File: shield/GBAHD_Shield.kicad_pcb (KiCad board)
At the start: 2 copper layers, 49 x 39 mm, 18 parts, among them J1 Conn_01x40, J2 Conn_02x08_Top_Bottom, J3 Conn_01x16, J4 Conn_02x10_Top_Bottom, J5 Conn_01x05, J6 Conn_02x03_Odd_Even, J7 Conn_01x01, SW1 SW_Push, U1 SNES_7PIN, U2 ATmega328P-AU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

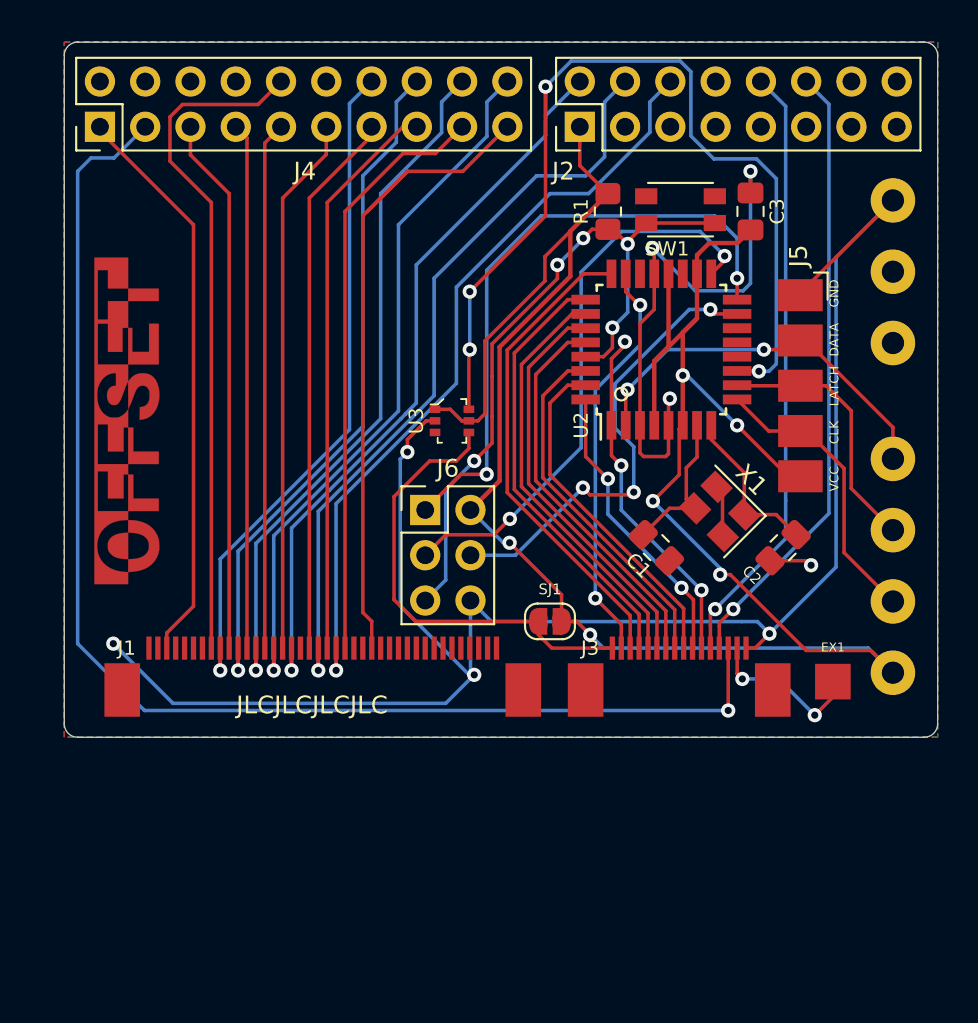
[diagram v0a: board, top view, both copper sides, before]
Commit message: Version 2 initial commit.
- Changed board layout
- Changed breakout board pin order
- Changed FFC connectors
- Added connectors for 32 pin and 34 pin
- Changed SNES connector to Classic connector.
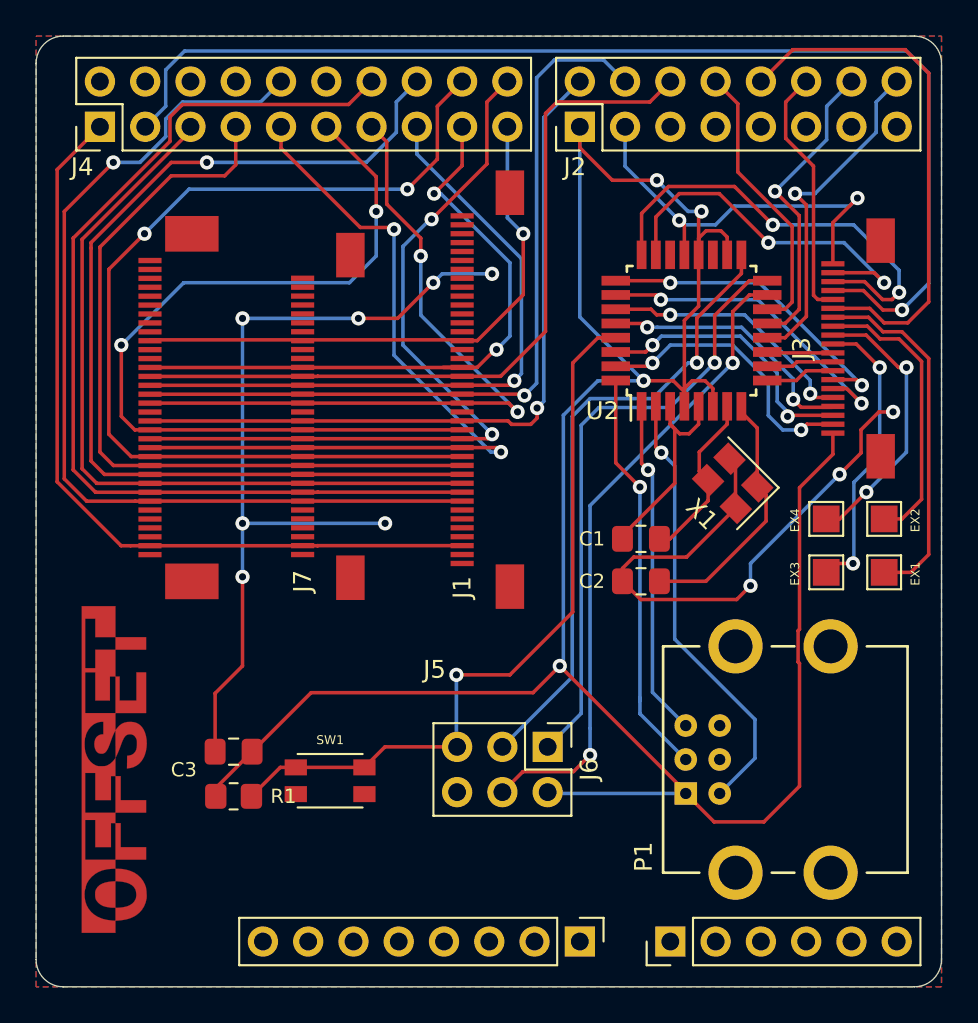
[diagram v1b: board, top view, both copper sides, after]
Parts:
- removed the G*** at (47.7, 47.8)
- removed SJ1: SOLDER_JUMPER, Jumper:SolderJumper-2_P1.3mm_Open_RoundedPad1.0x1.5mm
- removed U1: SNES_7PIN, OFFSET:SNES_7PIN
- removed U3: WAS3157B, OFFSET:SOT-363
- added G***: LOGO, Raizu_OFFSET:OFFSET_LOGO_4.0mm, F.Cu at (47.0, 67.3)
- added P1: CONN_WII, Raizu_OFFSET:CONN_WII, F.Cu at (84.5, 66.8)
- added REF**: PinHeader_1x06_P2.54mm_Vertical, Connector_PinHeader_2.54mm:PinHeader_1x06_P2.54mm_Vertical, F.Cu at (78.0, 77.0)
- added REF**: PinHeader_1x08_P2.54mm_Vertical, Connector_PinHeader_2.54mm:PinHeader_1x08_P2.54mm_Vertical, F.Cu at (72.9, 77.0)
- added TP1: EX1, TestPoint:TestPoint_Pad_1.5x1.5mm, F.Cu at (90.0, 56.2)
- added TP2: EX2, TestPoint:TestPoint_Pad_1.5x1.5mm, F.Cu at (90.0, 53.2)
- added TP3: EX3, TestPoint:TestPoint_Pad_1.5x1.5mm, F.Cu at (86.8, 56.2)
- added TP4: EX4, TestPoint:TestPoint_Pad_1.5x1.5mm, F.Cu at (86.8, 53.2)
- J1: footprint OFFSET:JUSHUO_AFC07-S40FCC-00 -> Raizu:JUSHUO_AFC01-S40FCC-00
- J3: value Conn_01x16 -> Conn_01x20; footprint OFFSET:JUSHUO_AFC07-S16FCC-00 -> Raizu:JUSHUO_AFC01-S20FCC-00
- J5: value Conn_01x05 -> Conn_01x34; footprint OFFSET:Pads_01x05 -> Raizu:JUSHUO_AFC07-S34FCC-00
- J7: value Conn_01x01 -> Conn_01x32; footprint OFFSET:SOLDER_PAD -> Raizu:JUSHUO_AFC01-S32FCC-00
- SW1: footprint OFFSET:XKB-TS-1185EC-C-D-B -> Raizu_OFFSET:XKB-TS-1185EC-C-D-B
- moved C3 41.9 mm to (53.5, 66.3), turned to 0 degrees
- moved R1 39.0 mm to (53.5, 68.8), turned to 0 degrees
- moved SW1 37.6 mm to (58.9, 67.9), turned to 0 degrees
- moved J5 34.5 mm to (50.6, 47.0), turned to 90 degrees
- moved J7 33.2 mm to (57.4, 47.5), turned to 90 degrees
- moved J3 20.5 mm to (87.1, 43.7), turned to 90 degrees
- moved J1 17.9 mm to (66.3, 46.5), turned to 90 degrees
- moved J6 15.0 mm to (71.1, 66.0), turned to 270 degrees
- moved C2 8.19 mm to (76.4, 56.8), turned to 0 degrees
- moved U2 2.00 mm to (79.2, 42.7)
- moved X1 1.74 mm to (81.5, 51.2)
- moved C1 0.99 mm to (76.4, 54.4), turned to 0 degrees
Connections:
- C3 pad 2: SP_3V3 -> GBA_VCC
- J2 pad 1: SP_3V3 -> GBA_VCC
- J3 pad 10: GBA_START -> GBA_RESET
- J3 pad 11: GBA_SELECT -> Net-(J3-Pad11)
- J3 pad 12: GBA_AUD2 -> Net-(J3-Pad12)
- J3 pad 13: GBA_AUD1 -> Net-(J3-Pad13)
- J3 pad 14: GBA_CLK -> Net-(J3-Pad14)
- J3 pad 15: Net-(J3-Pad15) -> GBA_AUD2
- J3 pad 16: GND -> GBA_AUD1
- J3 pad 2: GBA_UP -> GBA_R
- J3 pad 3: GBA_DOWN -> GBA_L
- J3 pad 4: GBA_LEFT -> GBA_B
- J3 pad 5: GBA_RGHT -> GBA_A
- J3 pad 6: GBA_A -> GBA_RGHT
- J3 pad 7: GBA_B -> GBA_LEFT
- J3 pad 8: GBA_L -> GBA_START
- J3 pad 9: GBA_R -> GBA_SELECT
- J5 pad 1: GND -> Net-(J5-Pad1)
- J5 pad 2: SNS_DATA -> GB_DCLK
- J5 pad 3: SNS_LATCH -> Net-(J5-Pad3)
- J5 pad 4: SNS_CLK -> Net-(J5-Pad4)
- J5 pad 5: SP_3V3 -> Net-(J5-Pad5)
- J6 pad 2: SP_3V3 -> GBA_VCC
- J7 pad 1: Net-(J3-Pad15) -> Net-(J7-Pad1)
- R1 pad 1: SP_3V3 -> GBA_VCC
- U2 pad 1: GBA_SELECT -> JOY_SDA
- U2 pad 10: SNS_LATCH -> GBA_SELECT
- U2 pad 11: GBA_POWER_SEL -> GBA_RESET
- U2 pad 12: Net-(U2-Pad12) -> SP_ARD0
- U2 pad 13: Net-(U2-Pad13) -> SP_ARD1
- U2 pad 14: Net-(U2-Pad14) -> SP_ARD4
- U2 pad 18: SP_3V3 -> GBA_VCC
- U2 pad 2: SNS_DATA -> JOY_SCL
- U2 pad 20: SP_3V3 -> GBA_VCC
- U2 pad 32: GBA_START -> JOY_DET
- U2 pad 4: SP_3V3 -> GBA_VCC
- U2 pad 6: SP_3V3 -> GBA_VCC
- U2 pad 9: SNS_CLK -> GBA_START
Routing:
- net SP_3V3: track 126.4 -> 0.00 mm, vias 6 -> 0
- net GBA_VCC: track 25.8 -> 136.2 mm, vias 0 -> 4
- net GBA_POWER_SEL: track 52.9 -> 0.00 mm, vias 4 -> 0
- net JOY_SCL: track 0.00 -> 25.1 mm, vias 0 -> 1
- net JOY_DET: track 0.00 -> 23.1 mm, vias 0 -> 1
- net SNS_DATA: track 21.9 -> 0.00 mm, vias 2 -> 0
- net GBA_AUD1: track 34.9 -> 14.3 mm, vias 1 -> 0
- net Net-(J3-Pad14): track 0.00 -> 20.2 mm
- net SP_ARD0: track 0.00 -> 19.2 mm, vias 0 -> 1
- net JOY_SDA: track 0.00 -> 18.9 mm, vias 0 -> 1
- net GB_R4: track 37.8 -> 56.5 mm, vias 1 -> 0
- net GB_R2: track 38.4 -> 56.4 mm
- net GND: track 134.3 -> 116.4 mm, vias 8 -> 12
- net GB_G2: track 30.3 -> 48.2 mm, vias 0 -> 2
- net SP_ARD1: track 0.00 -> 17.2 mm, vias 0 -> 1
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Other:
- board size 49 x 39 mm -> 50.8 x 53.3 mm
- board text removed: "CLK"
- board text removed: "DATA"
- board text removed: "Designed in México"
- board text removed: "EX1"
- board text removed: "GND"
- board text removed: "JLCJLCJLCJLC"
- board text removed: "LATCH"
- board text removed: "Raizu 2020"
- board text removed: "VCC"
- board text removed: "gbaHD Shield"

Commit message: PCB changes and breakout board
- Added breakout to main board as a breakaway board.
- Added controller connector expansion for port relocation
- Tidying routing and other minimal changes
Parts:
- removed the REF** at (72.9, 77.0)
- added CLK: GBA_CLK, Raizu_OFFSET:SOLDER_PAD, F.Cu at (21.8, 77.9)
- added GEX1: GBA_EX1, Raizu_OFFSET:SOLDER_PAD, F.Cu at (29.4, 61.0)
- added GEX2: GBA_EX2, Raizu_OFFSET:SOLDER_PAD, F.Cu at (22.0, 67.4)
- added GEX3: GBA_EX3, Raizu_OFFSET:SOLDER_PAD, F.Cu at (22.0, 70.0)
- added GEX4: GBA_EX4, Raizu_OFFSET:SOLDER_PAD, F.Cu at (22.0, 68.7)
- added GND: GBA_GND, Raizu_OFFSET:SOLDER_PAD, F.Cu at (24.1, 63.5)
- added J8: Conn_01x05, Connector_PinHeader_2.54mm:PinHeader_1x05_P2.54mm_Vertical, F.Cu at (42.1, 38.9)
- added J9: Conn_01x20, Raizu:JUSHUO_AFC01-S20FCC-00, F.Cu at (31.7, 69.5)
- added JP1: Jumper_NC_Small, Jumper:SolderJumper-2_P1.3mm_Bridged_RoundedPad1.0x1.5mm, B.Cu at (90.2, 34.8)
- added JP2: Jumper_NC_Small, Jumper:SolderJumper-2_P1.3mm_Bridged_RoundedPad1.0x1.5mm, B.Cu at (87.2, 34.8)
- added JP3: Jumper_NC_Small, Jumper:SolderJumper-2_P1.3mm_Bridged_RoundedPad1.0x1.5mm, B.Cu at (81.8, 34.8)
- added RESET: GBA_RESET, Raizu_OFFSET:SOLDER_PAD, F.Cu at (24.3, 75.0)
- added S01: GBA_S01, Raizu_OFFSET:SOLDER_PAD, F.Cu at (27.4, 61.0)
- added S02: GBA_S02, Raizu_OFFSET:SOLDER_PAD, F.Cu at (28.4, 63.5)
- added TP0: GBA_A, Raizu_OFFSET:SOLDER_PAD, F.Cu at (25.4, 61.0)
- added TP1: GBA_B, Raizu_OFFSET:SOLDER_PAD, F.Cu at (26.4, 63.5)
- added TP2: GBA_SEL, Raizu_OFFSET:SOLDER_PAD, F.Cu at (28.6, 77.6)
- added TP3: GBA_STR, Raizu_OFFSET:SOLDER_PAD, F.Cu at (26.9, 77.6)
- added TP4: GBA_DR, Raizu_OFFSET:SOLDER_PAD, F.Cu at (26.0, 75.0)
- added TP5: GBA_DL, Raizu_OFFSET:SOLDER_PAD, F.Cu at (23.5, 77.6)
- added TP6: GBA_DU, Raizu_OFFSET:SOLDER_PAD, F.Cu at (25.2, 77.6)
- added TP7: GBA_DD, Raizu_OFFSET:SOLDER_PAD, F.Cu at (27.7, 75.0)
- added TP8: GBA_R, Raizu_OFFSET:SOLDER_PAD, F.Cu at (23.4, 61.0)
- added TP9: GBA_L, Raizu_OFFSET:SOLDER_PAD, F.Cu at (22.6, 75.0)
- added VCC: GBA_VCC, Raizu_OFFSET:SOLDER_PAD, F.Cu at (30.3, 77.3)
- added mouse-bite-2.54mm-slot: VAL**, Panelization:mouse-bite-2.54mm-slot, F.Cu at (38.5, 64.2)
- added mouse-bite-2.54mm-slot: VAL**, Panelization:mouse-bite-2.54mm-slot, F.Cu at (38.5, 74.8)
- moved G*** 2.75 mm to (44.2, 67.5)
- renumbered TP1 to EX1, TP2 to EX2, TP3 to EX3, TP4 to EX4
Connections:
- U2 pad 12: SP_ARD0 -> Net-(JP1-Pad1)
- U2 pad 13: SP_ARD1 -> Net-(JP2-Pad1)
- U2 pad 14: SP_ARD4 -> Net-(JP3-Pad1)
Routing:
- net JOY_SDA: track 18.9 -> 80.2 mm, vias 1 -> 2
- net JOY_SCL: track 25.1 -> 85.4 mm, vias 1 -> 2
- net JOY_DET: track 23.1 -> 82.4 mm, vias 1 -> 2
- net GBA_VCC: track 136.2 -> 169.7 mm, vias 4 -> 5
- net Net-(J9-Pad2): track 0.00 -> 31.2 mm, vias 0 -> 2
- net Net-(GBA3-Pad1): track 0.00 -> 30.7 mm, vias 0 -> 2
- net Net-(J9-Pad19): track 0.00 -> 28.4 mm, vias 0 -> 2
- net Net-(J9-Pad5): track 0.00 -> 23.5 mm, vias 0 -> 2
- net Net-(GEX1-Pad1): track 0.00 -> 19.3 mm, vias 0 -> 2
- net Net-(J9-Pad16): track 0.00 -> 17.8 mm, vias 0 -> 2
- net Net-(J9-Pad18): track 0.00 -> 16.5 mm, vias 0 -> 2
- net Net-(JP1-Pad1): track 0.00 -> 16.4 mm, vias 0 -> 1
- net Net-(J9-Pad15): track 0.00 -> 15.6 mm, vias 0 -> 2
- net GND: track 116.4 -> 130.2 mm, vias 12 -> 17
- net Net-(J9-Pad3): track 0.00 -> 13.7 mm, vias 0 -> 2
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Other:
- board size 50.8 x 53.3 mm -> 72.3 x 53.3 mm
- board text added: "JLCJLCJLCJLC"
- board text added: "Raizu 2021 Designed in México"
- board text added: "gbaHD Shield"

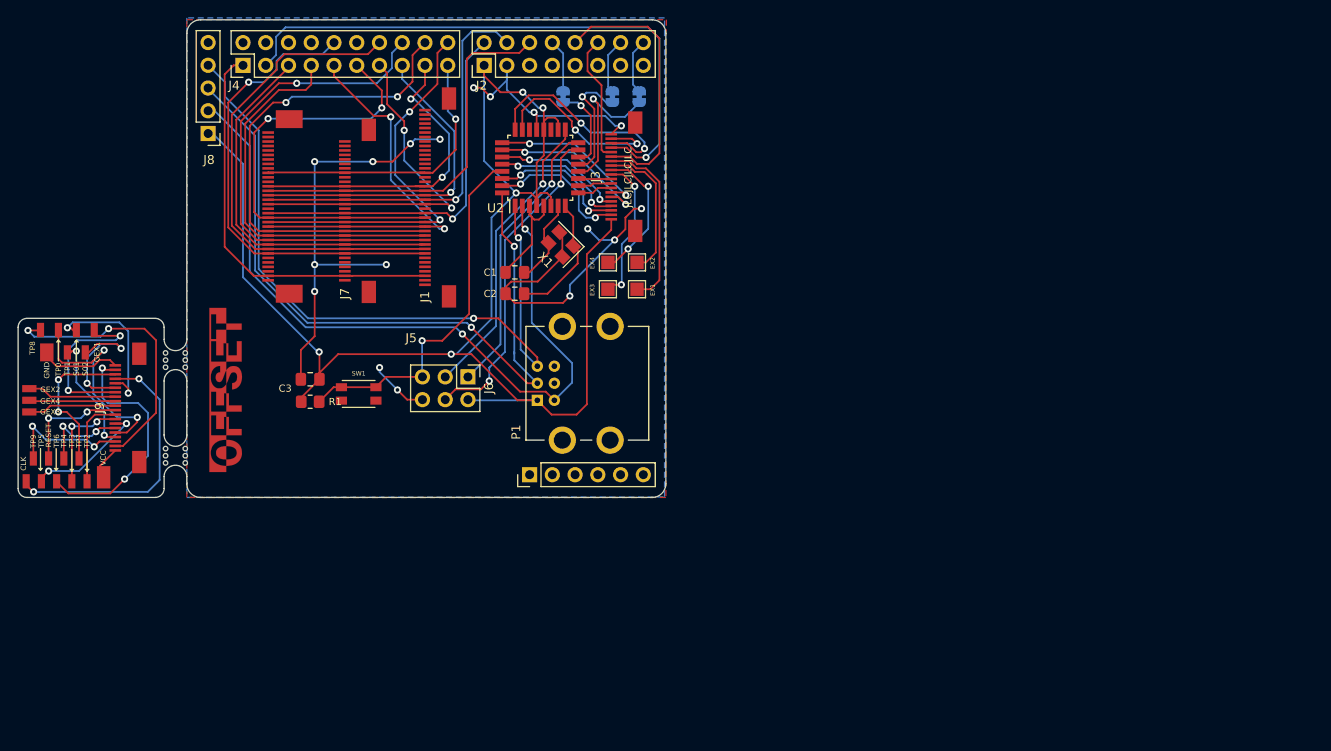
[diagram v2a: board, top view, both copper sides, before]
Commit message: PCB design work
- Added extension board (controller, LED and power switch)
- Panelized board
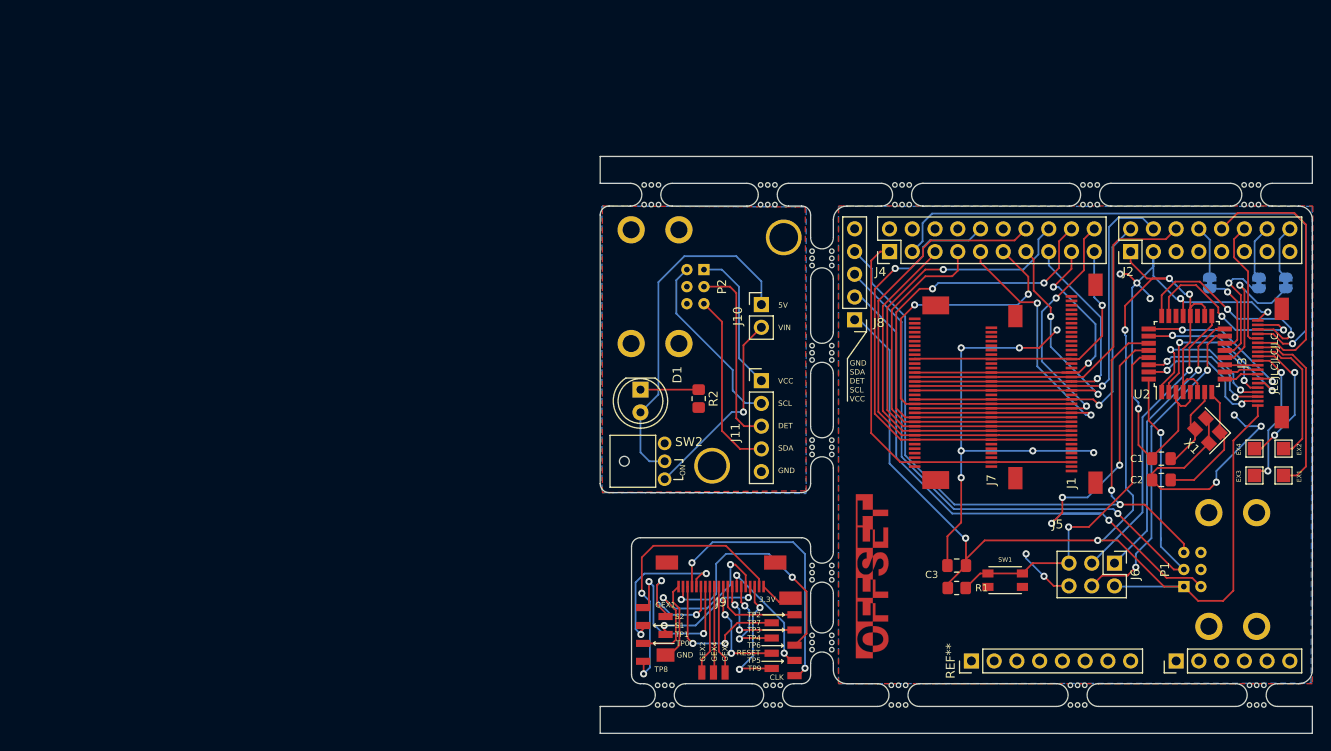
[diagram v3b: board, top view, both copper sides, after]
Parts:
- removed CLK: GBA_CLK, Raizu_OFFSET:SOLDER_PAD
- removed GND: GBA_GND, Raizu_OFFSET:SOLDER_PAD
- removed RESET: GBA_RESET, Raizu_OFFSET:SOLDER_PAD
- removed S01: GBA_S01, Raizu_OFFSET:SOLDER_PAD
- removed S02: GBA_S02, Raizu_OFFSET:SOLDER_PAD
- removed VCC: GBA_VCC, Raizu_OFFSET:SOLDER_PAD
- removed the mouse-bite-2.54mm-slot at (38.5, 64.2)
- removed the mouse-bite-2.54mm-slot at (38.5, 74.8)
- added D1: LED, LED_THT:LED_D5.0mm_FlatTop, F.Cu at (90.4, 67.5)
- added GBA1: GBA_VCC, Raizu_OFFSET:SOLDER_PAD, F.Cu at (107.1, 90.9)
- added GBA2: GBA_RESET, Raizu_OFFSET:SOLDER_PAD, F.Cu at (104.9, 96.9)
- added GBA3: GBA_CLK, Raizu_OFFSET:SOLDER_PAD, F.Cu at (107.7, 99.4)
- added GBA4: GBA_GND, Raizu_OFFSET:SOLDER_PAD, F.Cu at (93.3, 97.1)
- added HOLE_M3: VAL**, keyboard_parts:HOLE_M3, F.Cu at (98.4, 76.0)
- added HOLE_M3: VAL**, keyboard_parts:HOLE_M3, F.Cu at (106.4, 50.5)
- added J10: Conn_01x02, Connector_PinHeader_2.54mm:PinHeader_1x02_P2.54mm_Vertical, F.Cu at (103.9, 58.0)
- added J11: Conn_01x05, Connector_PinHeader_2.54mm:PinHeader_1x05_P2.54mm_Vertical, F.Cu at (103.9, 66.5)
- added P2: CONN_WII, Raizu_OFFSET:CONN_WII, F.Cu at (91.9, 56.0)
- added R2: 120, Resistor_SMD:R_0805_2012Metric_Pad1.20x1.40mm_HandSolder, F.Cu at (96.9, 68.5)
- added REF**: PinHeader_1x08_P2.54mm_Vertical, Connector_PinHeader_2.54mm:PinHeader_1x08_P2.54mm_Vertical, F.Cu at (127.3, 97.8)
- added S1: GBA_S01, Raizu_OFFSET:SOLDER_PAD, F.Cu at (90.8, 93.8)
- added S2: GBA_S02, Raizu_OFFSET:SOLDER_PAD, F.Cu at (93.3, 92.8)
- added SW2: Switch-DPDT, Raizu_OFFSET:XKB_XKB5858-Z-C, F.Cu at (90.9, 75.5)
- added mouse-bite-2.54mm-slot: VAL**, Panelization:mouse-bite-2.54mm-slot, F.Cu at (140.6, 45.7)
- added mouse-bite-2.54mm-slot: VAL**, Panelization:mouse-bite-2.54mm-slot, F.Cu at (93.1, 101.6)
- added mouse-bite-2.54mm-slot: VAL**, Panelization:mouse-bite-2.54mm-slot, F.Cu at (110.7, 95.7)
- added mouse-bite-2.54mm-slot: VAL**, Panelization:mouse-bite-2.54mm-slot, F.Cu at (110.7, 87.9)
- added mouse-bite-2.54mm-slot: VAL**, Panelization:mouse-bite-2.54mm-slot, F.Cu at (110.7, 52.8)
- added mouse-bite-2.54mm-slot: VAL**, Panelization:mouse-bite-2.54mm-slot, F.Cu at (110.7, 63.4)
- added mouse-bite-2.54mm-slot: VAL**, Panelization:mouse-bite-2.54mm-slot, F.Cu at (110.7, 73.9)
- added mouse-bite-2.54mm-slot: VAL**, Panelization:mouse-bite-2.54mm-slot, F.Cu at (158.6, 45.7)
- added mouse-bite-2.54mm-slot: VAL**, Panelization:mouse-bite-2.54mm-slot, F.Cu at (119.6, 45.7)
- added mouse-bite-2.54mm-slot: VAL**, Panelization:mouse-bite-2.54mm-slot, F.Cu at (104.6, 45.7)
- added mouse-bite-2.54mm-slot: VAL**, Panelization:mouse-bite-2.54mm-slot, F.Cu at (91.6, 45.7)
- added mouse-bite-2.54mm-slot: VAL**, Panelization:mouse-bite-2.54mm-slot, F.Cu at (139.2, 101.6)
- added mouse-bite-2.54mm-slot: VAL**, Panelization:mouse-bite-2.54mm-slot, F.Cu at (159.2, 101.6)
- added mouse-bite-2.54mm-slot: VAL**, Panelization:mouse-bite-2.54mm-slot, F.Cu at (119.2, 101.6)
- added mouse-bite-2.54mm-slot: VAL**, Panelization:mouse-bite-2.54mm-slot, F.Cu at (105.2, 101.6)
- moved TP5 86.3 mm to (107.4, 97.7), turned to 90 degrees
- moved TP9 85.6 mm to (104.9, 98.6), turned to 90 degrees
- moved TP6 84.3 mm to (107.4, 96.0), turned to 90 degrees
- moved GEX3 83.2 mm to (99.8, 99.2), turned to 180 degrees
- moved GEX4 82.4 mm to (98.5, 99.2), turned to 180 degrees
- moved TP3 82.3 mm to (107.4, 94.3), turned to 90 degrees
- moved GEX2 81.7 mm to (97.2, 99.2), turned to 180 degrees
- moved TP4 81.4 mm to (104.9, 95.2), turned to 90 degrees
- moved TP2 80.3 mm to (107.4, 92.6), turned to 90 degrees
- moved TP7 79.4 mm to (104.9, 93.5), turned to 90 degrees
- moved TP8 76.9 mm to (90.8, 97.8), turned to 270 degrees
- moved SW1 75.1 mm to (131.1, 88.7)
- moved C1 75.1 mm to (148.6, 75.2)
- moved C2 75.1 mm to (148.6, 77.5)
- moved C3 75.1 mm to (125.7, 87.1)
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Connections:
- U2 pad 1: JOY_SDA -> GBA_B
- U2 pad 2: JOY_SCL -> GBA_A
- U2 pad 27: GBA_A -> JOY_SDA
- U2 pad 28: GBA_B -> JOY_SCL
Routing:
- net EXT_5V: track 0.00 -> 39.4 mm
- net EXT_VIN: track 0.00 -> 22.2 mm, vias 0 -> 1
- net GND: track 130.2 -> 151.5 mm, vias 17 -> 18
- net EXT_DET: track 0.00 -> 21.1 mm
- net EXT_SCL: track 0.00 -> 20.4 mm
- net EXT_SDA: track 0.00 -> 20.3 mm
- net EXT_3V3: track 0.00 -> 16.2 mm
- net JOY_SCL: track 85.4 -> 92.7 mm, vias 2 -> 4
- net Net-(D1-Pad1): track 0.00 -> 6.50 mm
- net GBA_VCC: track 169.7 -> 164.0 mm
- net GBA_A: track 14.7 -> 18.0 mm
- net GBA_B: track 14.8 -> 17.8 mm
- net JOY_SDA: track 80.2 -> 82.7 mm
- added copper zone on B.Cu, net EXT_GND
- added copper zone on F.Cu, net EXT_GND
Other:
- board size 72.3 x 53.3 mm -> 79.5 x 64.4 mm
- board text added: "3.3V"
- board text added: "5V"
- board text added: "CLK"
- board text added: "DET"
- board text added: "GND"
- board text added: "ON"
- board text added: "RESET"
- board text added: "SCL"
- board text added: "SDA"
- board text added: "VCC"
- board text added: "VIN"
